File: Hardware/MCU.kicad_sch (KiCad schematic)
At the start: 37 parts, among them J5 Conn_01x05_Pin, Q1 BC847, SW1 SW_Push, SW2 SW_SPDT, U1 STM32F405RGT6, Y2 25MHz

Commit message: Added Impedance matching calculations, finished buck converter calculations, finalized buzzer circuitry
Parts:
- FB1: footprint (none) -> Resistor_SMD:R_0603_1608Metric; Distributer Link (none) -> https://www.e-komponent.com/blm18he601sn1d-murata-electroni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; Part Number (none) -> BLM18HE601SN1D
- Q1: Distributer Link https://www.ozdisan.com/p/discrete-transistorler-442/onsem-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 -> https://www.e-komponent.com/bc817-40w-r1-00001-panjit-inter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; Part Number BC847CWT1G -> BC817-40W_R1_00001
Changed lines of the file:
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@@
 			)
 		)
-		(property "Distributer Link" "https://www.ozdisan.com/p/discrete-transistorler-442/onsem-bc847cwt1g-1594721"
+		(property "Distributer Link" "https://www.e-komponent.com/bc817-40w-r1-00001-panjit-international-bipolar-transistor-tekli"
 			(at 261.493 118.364 0)
 			(hide yes)
@@
 			)
 		)
-		(property "Part Number" "BC847CWT1G"
+		(property "Part Number" "BC817-40W_R1_00001 "
 			(at 261.493 118.364 0)
 			(hide yes)
@@
 			)
 		)
-		(property "Footprint" ""
+		(property "Footprint" "Resistor_SMD:R_0603_1608Metric"
 			(at 265.43 69.342 90)
 			(hide yes)
@@
 			)
 		)
-		(property "Datasheet" ""
+		(property "Datasheet" "https://www.murata.com/en-us/products/productdata/8796741599262/ENFA0004.pdf"
 			(at 265.43 71.12 0)
 			(hide yes)
@@
 			(at 265.43 71.12 0)
 			(hide yes)
+			(show_name no)
+			(do_not_autoplace no)
+			(effects
+				(font
+					(size 1.27 1.27)
+				)
+			)
+		)
+		(property "Distributer Link" "https://www.e-komponent.com/blm18he601sn1d-murata-electronics-ferit-bead-ve-cip"
+			(at 265.43 71.12 0)
+			(hide yes)
+			(show_name no)
+			(do_not_autoplace no)
+			(effects
+				(font
+					(size 1.27 1.27)
+				)
+			)
+		)
+		(property "Part Number" "BLM18HE601SN1D"
+			(at 265.43 71.12 0)
+			(hide yes)

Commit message: Changed footprints, generated BOM
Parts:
- removed C1, C2, C3, C4, C5, C6, C7: 100nF, Capacitor_SMD:C_0402_1005Metric, symbol Device:C
- removed R26, R28: 10k, Resistor_SMD:R_0402_1005Metric, symbol Device:R
- removed R9: 1k, Resistor_SMD:R_0402_1005Metric, symbol Device:R
- added C21, C23, C24, C25, C38, C40, C41: 100nF, Capacitor_SMD:C_0603_1608Metric, symbol Device:C
- added R100, R75: 10k, Resistor_SMD:R_0603_1608Metric, symbol Device:R
- added R12: 1k, Resistor_SMD:R_0603_1608Metric, symbol Device:R
- C11, C17: footprint Capacitor_SMD:C_0402_1005Metric -> Capacitor_SMD:C_0603_1608Metric; Distributer Link https://www.ozdisan.com/p/smt-smd-ve-mlcc-kapasitorler-184/murata-grt155r71e104ke01d-1074547 -> https://www.ozdisan.com/p/smt-smd-ve-mlcc-kapasitorler-184/samsung-cl10b104ko8wpnc-522227; Part Number GRT155R71E104KE01D -> CL10B104KO8WPNC
- R10, R11: footprint Resistor_SMD:R_0402_1005Metric -> Resistor_SMD:R_0603_1608Metric; Distributer Link https://www.ozdisan.com/p/smt-smd-ve-cip-direncler-194/roya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 -> https://www.ozdisan.com/p/smt-smd-ve-cip-direncler-194/vish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; Part Number HP02WAF1001TCE -> CRCW06031K00JNTABC
- R27: footprint Resistor_SMD:R_0402_1005Metric -> Resistor_SMD:R_0603_1608Metric; Distributer Link https://www.ozdisan.com/p/smt-smd-ve-cip-direncler-194/royalohm-cq02wgj047jtce-587859 -> https://www.ozdisan.com/p/smt-smd-ve-cip-direncler-194/royalohm-cq03saf470kt5e-587940; Part Number CQ02WGJ047JTCE -> CQ03SAF470KT5E
- R4, R5: value 5.1k -> 4.7k; footprint Resistor_SMD:R_0402_1005Metric -> Resistor_SMD:R_0603_1608Metric; Distributer Link https://www.ozdisan.com/p/smt-smd-ve-cip-direncler-194/pana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 -> https://www.ozdisan.com/p/smt-smd-ve-cip-direncler-194/roya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; Part Number ERJ2RKF5101X -> CQ03SAJ0472T5E
- R53: footprint Resistor_SMD:R_0402_1005Metric -> Resistor_SMD:R_0603_1608Metric; Distributer Link https://www.ozdisan.com/p/smt-smd-ve-cip-direncler-194/roya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 -> https://www.ozdisan.com/p/smt-smd-ve-cip-direncler-194/viki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; Part Number CQ02WGF1002TCE -> CRT03J7E1002
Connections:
- net +3.3V: now also C21.1, C23.1, C24.1, C25.1, C38.1, C40.1, R100.2, R75.1
- net Blue_LED: now also R12.1
- net GND: now also C21.2, C23.2, C24.2, C25.2, C38.2, C40.2, C41.2
- net NRST: now also C11.1, R53.2, SW1.2
- net Sense_alert: now also R100.1
- net at D2.2 (A): now also R12.2
- net at SW2.1 (A): now also R75.2
- net at FB1.1: now also C41.1
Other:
- note removed: "consider a ferrite bead"
- moved on the sheet: BZ1, C10, C11, C12, C13, C14, C18, C45, D1, D2, D5, D6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

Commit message: :)
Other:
- moved on the sheet: BZ1, C10, C11, C17, C18, D1, D2, D5, D6, D7, J5, Q1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

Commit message: Changed oscillator footprint
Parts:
- Y2: footprint Crystal:Crystal_SMD_3225-4Pin_3.2x2.5mm -> Crystal:Crystal_SMD_2520-4Pin_2.5x2.0mm
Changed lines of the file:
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@@
 			)
 		)
-		(property "Footprint" "Crystal:Crystal_SMD_3225-4Pin_3.2x2.5mm"
+		(property "Footprint" "Crystal:Crystal_SMD_2520-4Pin_2.5x2.0mm"
 			(at 43.688 83.058 0)
 			(hide yes)

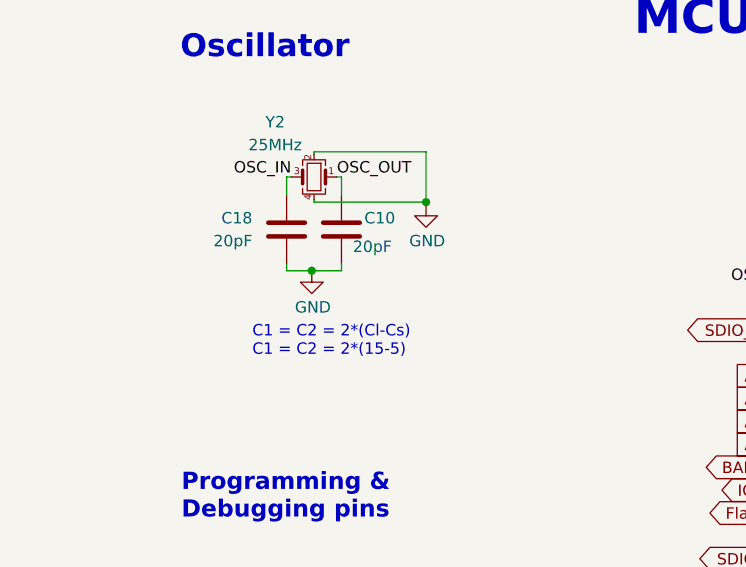
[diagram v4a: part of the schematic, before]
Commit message: Changed diff pair impedance calculation
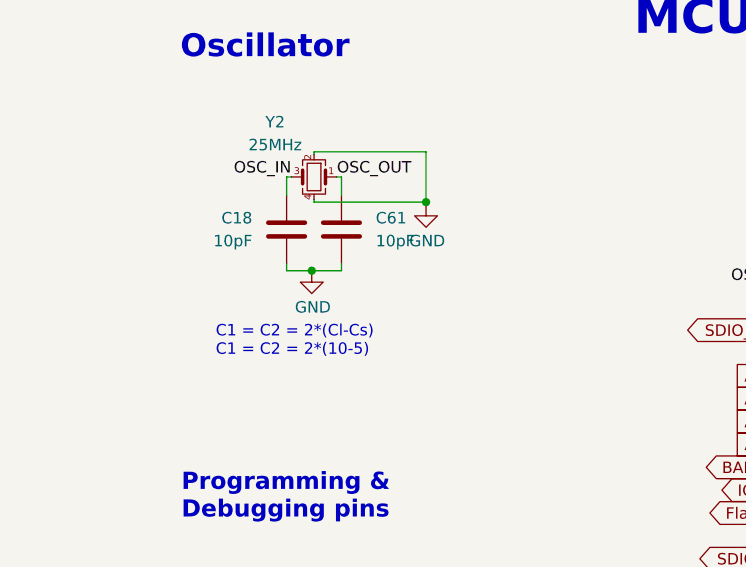
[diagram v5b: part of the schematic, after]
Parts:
- removed C10: 20pF, Capacitor_SMD:C_0603_1608Metric, symbol Device:C
- added C61: 10pF, Capacitor_SMD:C_0603_1608Metric, symbol Device:C
- C18: value 20pF -> 10pF; Distributer Link https://www.ozdisan.com/p/smt-smd-ve-mlcc-kapasitorler-184/yageo-cc0603jrnpo9bn200-747236 -> https://www.ozdisan.com/p/smt-smd-ve-mlcc-kapasitorler-184/samsung-cl10c100jb81pnc-522432; Part Number CC0603JRNPO9BN200 -> CL10C100JB81PNC
- Y2: Distributer Link https://www.ozdisan.com/p/osilatorler-510/raltron-com1305-2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 -> https://www.ozdisan.com/p/kristaller-508/ecs-ecs-250-10-36q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; Part Number COM1305-25.000-EXT-T-TR -> ECS-250-10-36Q-ES-TR
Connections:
- net GND: now also C61.2
- net OSC_OUT: now also C61.1
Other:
- note added: "C1 = C2 = 2*(Cl-Cs) C1 = C2 = 2*(10-5)"
- note removed: "C1 = C2 = 2*(Cl-Cs) C1 = C2 = 2*(15-5)"

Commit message: Added MOSFET simulation files with official spice model
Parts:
- added C46: 22uF, Capacitor_SMD:C_0805_2012Metric, symbol Device:C
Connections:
- net +5V: now also C46.1
- net GND: now also C46.2

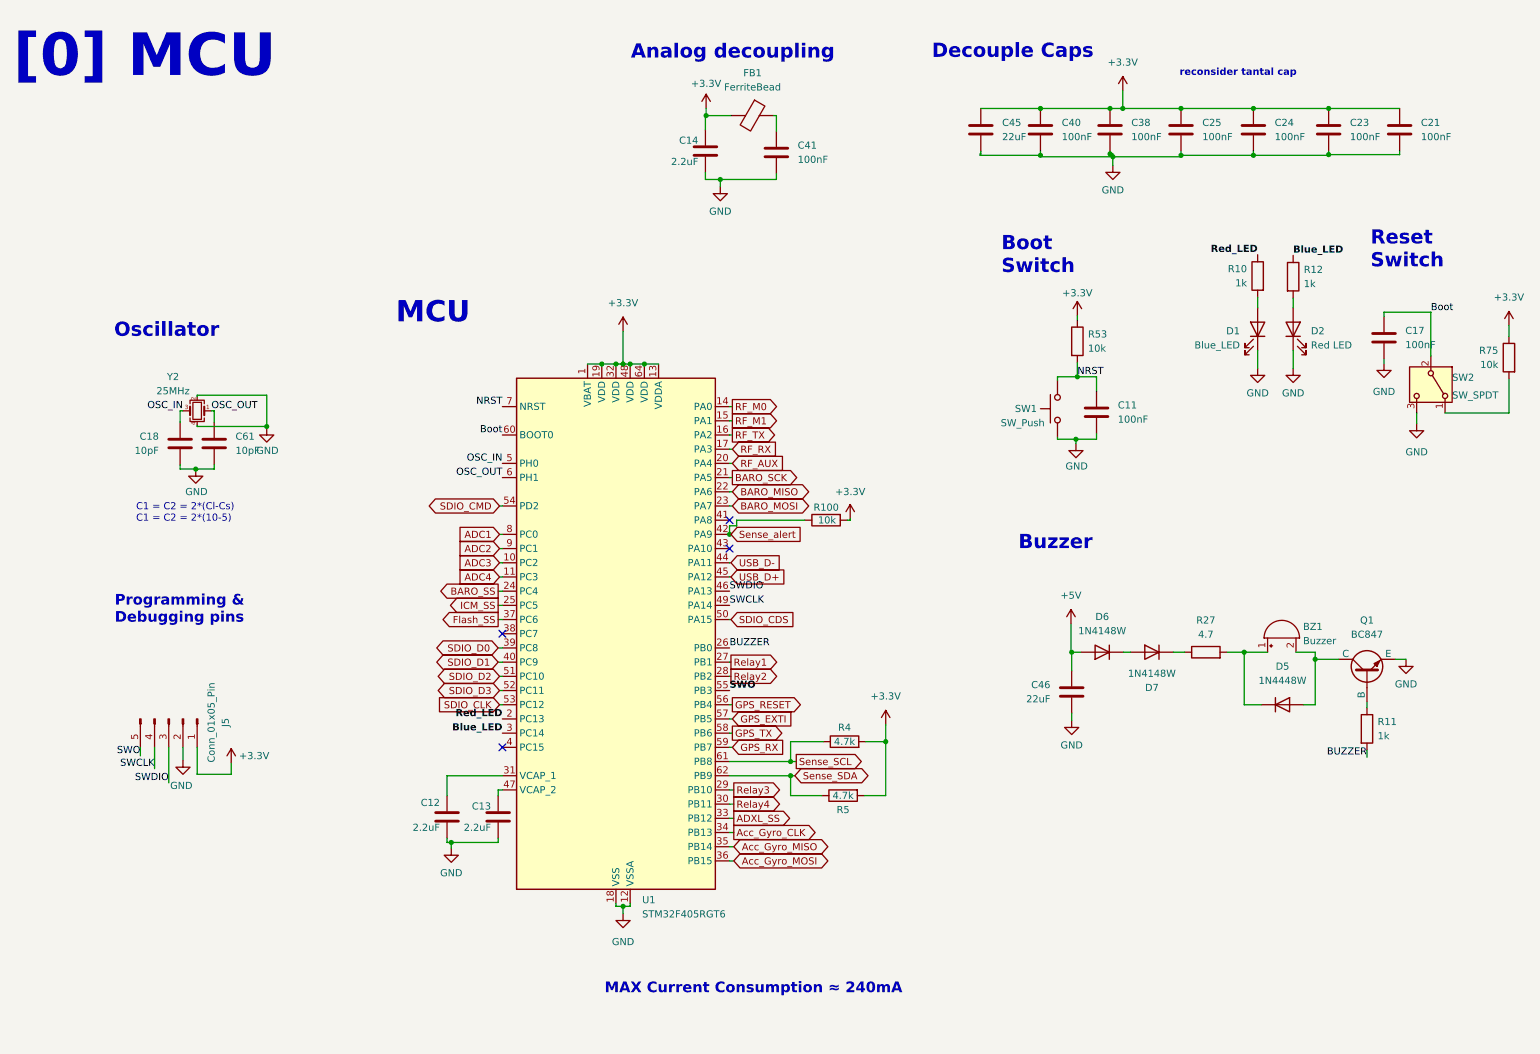
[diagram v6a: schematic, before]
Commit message: Purged heavy binaries and updated gitignore
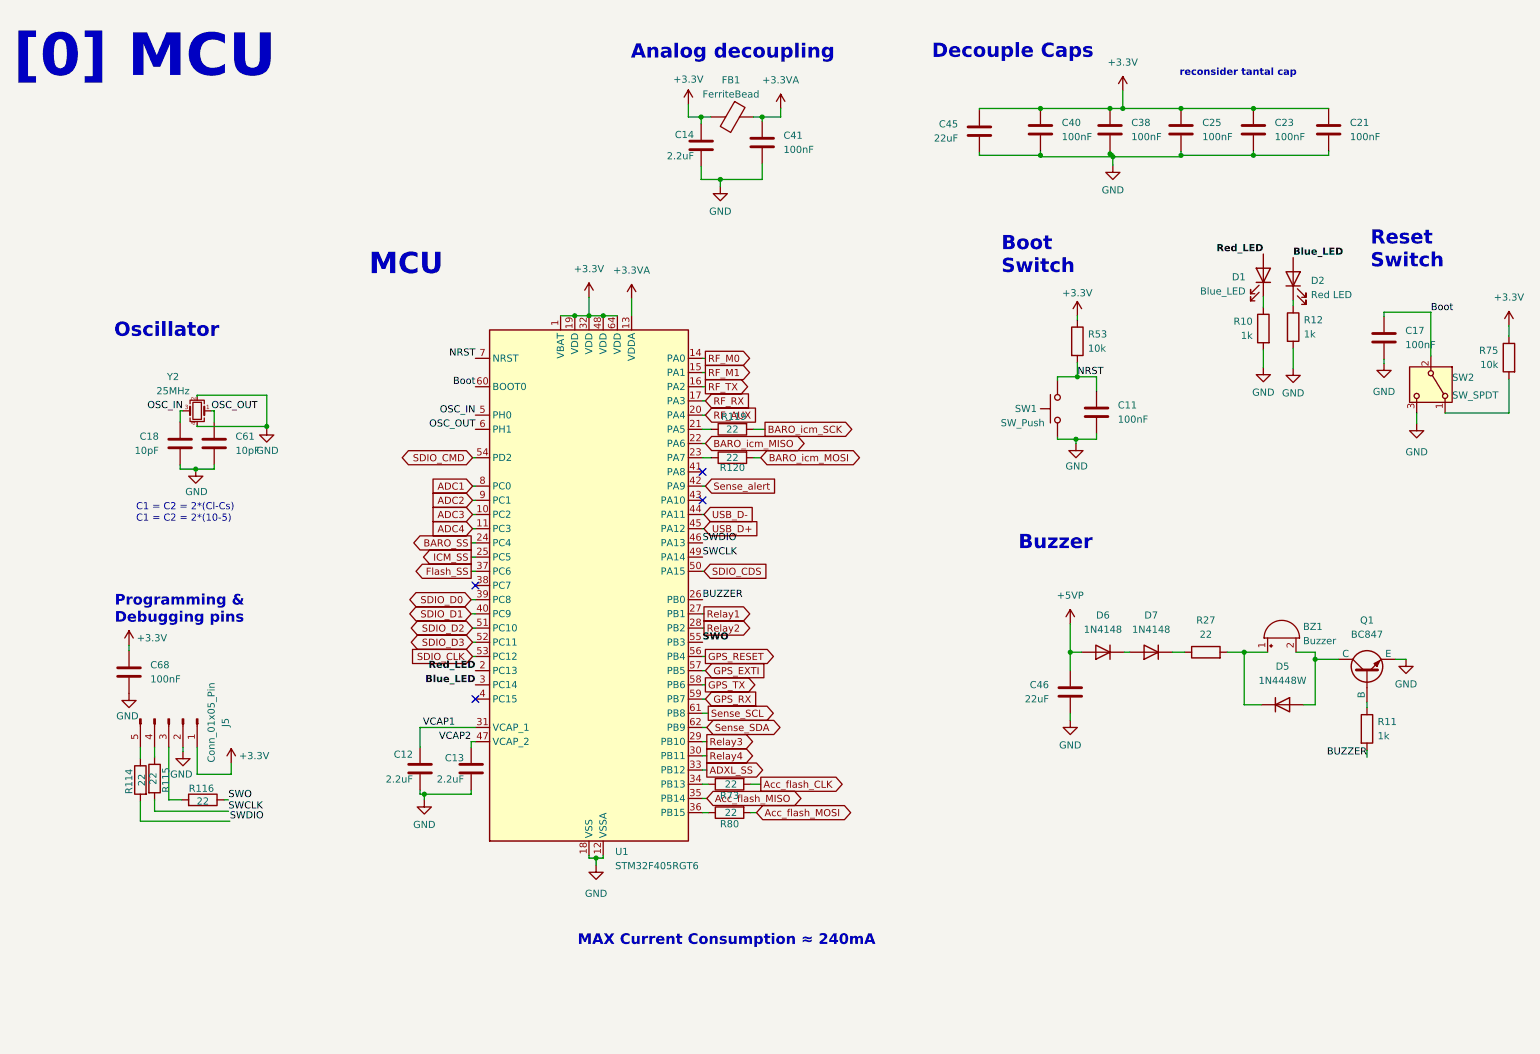
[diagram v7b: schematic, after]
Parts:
- removed C24: 100nF, Capacitor_SMD:C_0603_1608Metric, symbol Device:C
- removed D6, D7: 1N4148W, Diode_SMD:D_SOD-123, symbol Device:D
- removed R100: 10k, Resistor_SMD:R_0603_1608Metric, symbol Device:R
- removed R4, R5: 4.7k, Resistor_SMD:R_0603_1608Metric, symbol Device:R
- added C68: 100nF, Capacitor_SMD:C_0603_1608Metric, symbol Device:C
- added D6, D7: 1N4148, Diode_SMD:D_SOD-523, symbol Diode:1N4148WS
- added R114, R115, R116, R119, R120, R73, R80: 22, Resistor_SMD:R_0603_1608Metric, symbol Device:R
- FB1: Distributer Link https://www.e-komponent.com/blm18he601sn1d-murata-electroni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 -> https://www.mouser.com.tr/en/ProductDetail/Murata-Electroni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
- R27: value 4.7 -> 22; Distributer Link https://www.ozdisan.com/p/smt-smd-ve-cip-direncler-194/roya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 -> https://www.ozdisan.com/p/smt-smd-ve-cip-direncler-194/pana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; Part Number CQ03SAF470KT5E -> ERJPA3J220V
- SW1: Distributer Link https://www.ozdisan.com/p/tact-sivicler-485/littelfuse-ck-p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 -> https://www.mouser.com.tr/en/ProductDetail/CK/PTS815SJK250S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
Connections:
- net +3.3V: now also C68.1; no longer U1.13 (VDDA)
- net Blue_LED: now also D2.2 (A); no longer R12.1
- net GND: now also R10.2, R12.2, C68.2; no longer D1.1 (K), D2.1 (K)
- net Red_LED: now also D1.2 (A); no longer R10.1
- net SWCLK: now also R115.2; no longer J5.4 (Pin_4)
- net SWDIO: now also R114.2; no longer J5.3 (Pin_3)
- net SWO: now also R116.1; no longer J5.5 (Pin_5)
- net VCAP2: now reaches C13.1, U1.47 (VCAP_2)
- net +3.3VA: now reaches C41.1, FB1.1
- net +3.3VA: now also U1.13 (VDDA)
- net at R27.1: now also D7.1 (K)
- net VCAP1: now reaches C12.1, U1.31 (VCAP_1)
- net +5V renamed +5VP
- net +5VP: now also D6.2 (A)
- net Acc_Gyro_CLK: no longer names the net of U1.34 (PB13)
- net Acc_Gyro_CLK: now also R73.1
- net Acc_Gyro_MISO renamed Acc_flash_MISO
- net Acc_Gyro_MOSI: no longer names the net of U1.36 (PB15)
- net Acc_Gyro_MOSI: now also R80.1
- net BARO_MISO renamed BARO_icm_MISO
- net BARO_MOSI: no longer names the net of U1.23 (PA7)
- net BARO_MOSI: now also R120.1
- net BARO_SCK: no longer names the net of U1.21 (PA5)
- net BARO_SCK: now also R119.1
- new net: D2.1 (K), R12.1
- new net: J5.4 (Pin_4), R115.1
- new net: J5.3 (Pin_3), R116.2
- new net: J5.5 (Pin_5), R114.1
- new net: D1.1 (K), R10.1
- new net: D6.1 (K), D7.2 (A)
- new net Acc_flash_CLK: R73.2
- new net Acc_flash_MOSI: R80.2
- new net BARO_icm_MOSI: R120.2
- new net BARO_icm_SCK: R119.2
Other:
- moved on the sheet: C12, C13, C14, C21, C23, C41, D1, D2, FB1, R10, R12, U1
